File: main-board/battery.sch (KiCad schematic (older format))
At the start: 17 parts, among them Q301 DMG1012T, U301 SX1308, U302 DW06D

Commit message: refactor
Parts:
- added TP301: VBAT, TestPoint:TestPoint_Pad_D1.0mm, symbol Connector:TestPoint
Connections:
- net labels added: BAT_GND
- wire segments 50 -> 51
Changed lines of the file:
@@
 $Descr A4 11693 8268
 encoding utf-8
-Sheet 3 3
+Sheet 3 4
 Title ""
 Date ""
@@
 Text HLabel 6270 2330 2    50   Output ~ 0
 BATTERY_READ
+Text Label 1680 2080 2    50   ~ 0
+BAT_GND
+$Comp
+L Connector:TestPoint TP?
+U 1 1 5DA11FCB
+P 5160 4270
+AR Path="/5DA11FCB" Ref="TP?"  Part="1"
+AR Path="/5DC2722E/5DA11FCB" Ref="TP301"  Part="1"
+F 0 "TP301" V 5230 4440 50  0000 R CNN
+F 1 "VBAT" V 5070 4440 50  0000 R CNN
+F 2 "TestPoint:TestPoint_Pad_D1.0mm" H 5360 4270 50  0001 C CNN
+F 3 "~" H 5360 4270 50  0001 C CNN
+	1    5160 4270
+	0    -1   -1   0
+$EndComp
+Wire Wire Line
+	5160 4270 5360 4270
+Text Label 5190 4270 0    50   ~ 0
+VBAT
 $EndSCHEMATC

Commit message: ALPHA 1
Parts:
- added TP401: +3V3, TestPoint:TestPoint_Pad_D1.0mm, symbol Connector:TestPoint
- renumbered BT301 to BT401, C301 to C401, C303 to C402, C304 to C403, C302 to C404, D301 to D401, L301 to L401, Q301 to Q401, R301 to R401, R302 to R402, R304 to R403, R306 to R404, R307 to R405, R303 to R406, R305 to R407, TP301 to TP402, U301 to U401, U302 to U402
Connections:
- wire segments 51 -> 52
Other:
- moved on the sheet: BT401, C403, C404, Q401, R404, R405, R406, R407, TP402, U402

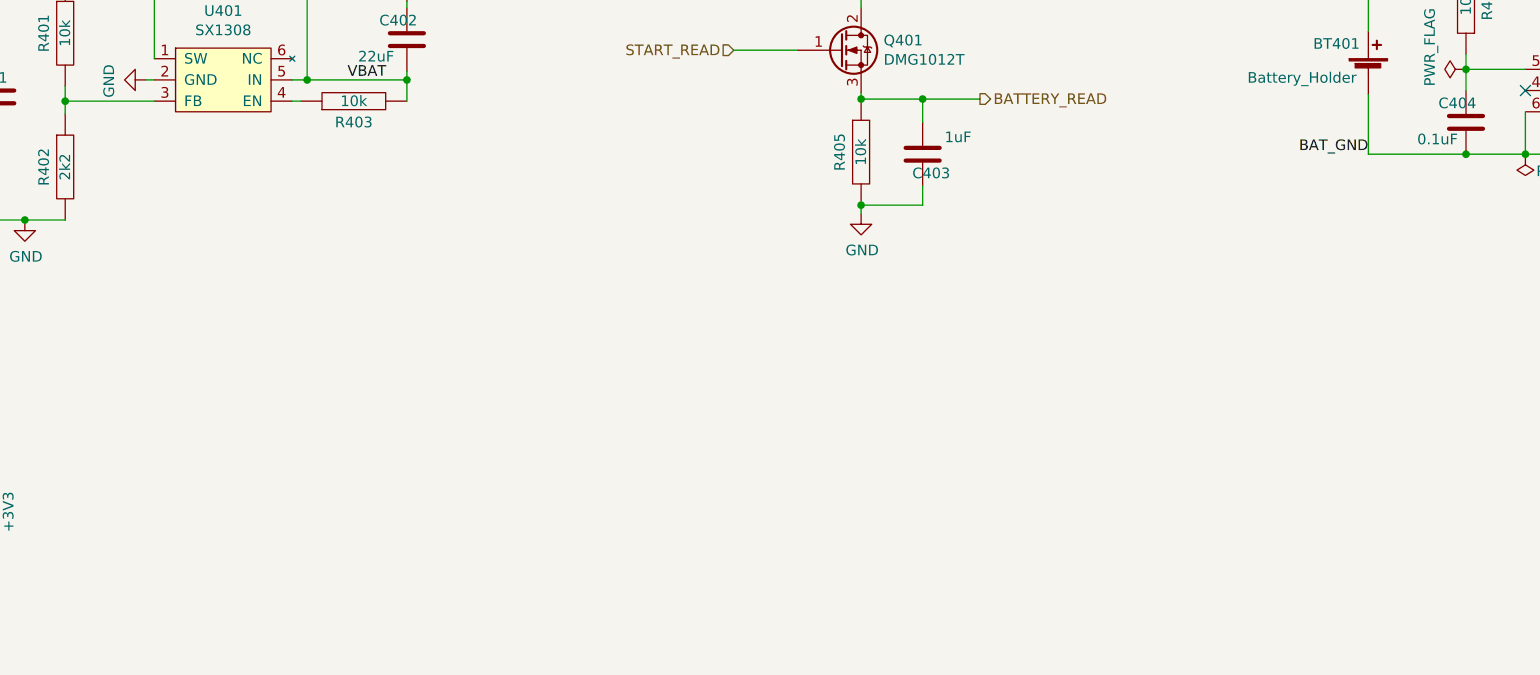
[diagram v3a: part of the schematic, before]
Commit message: added battery charging
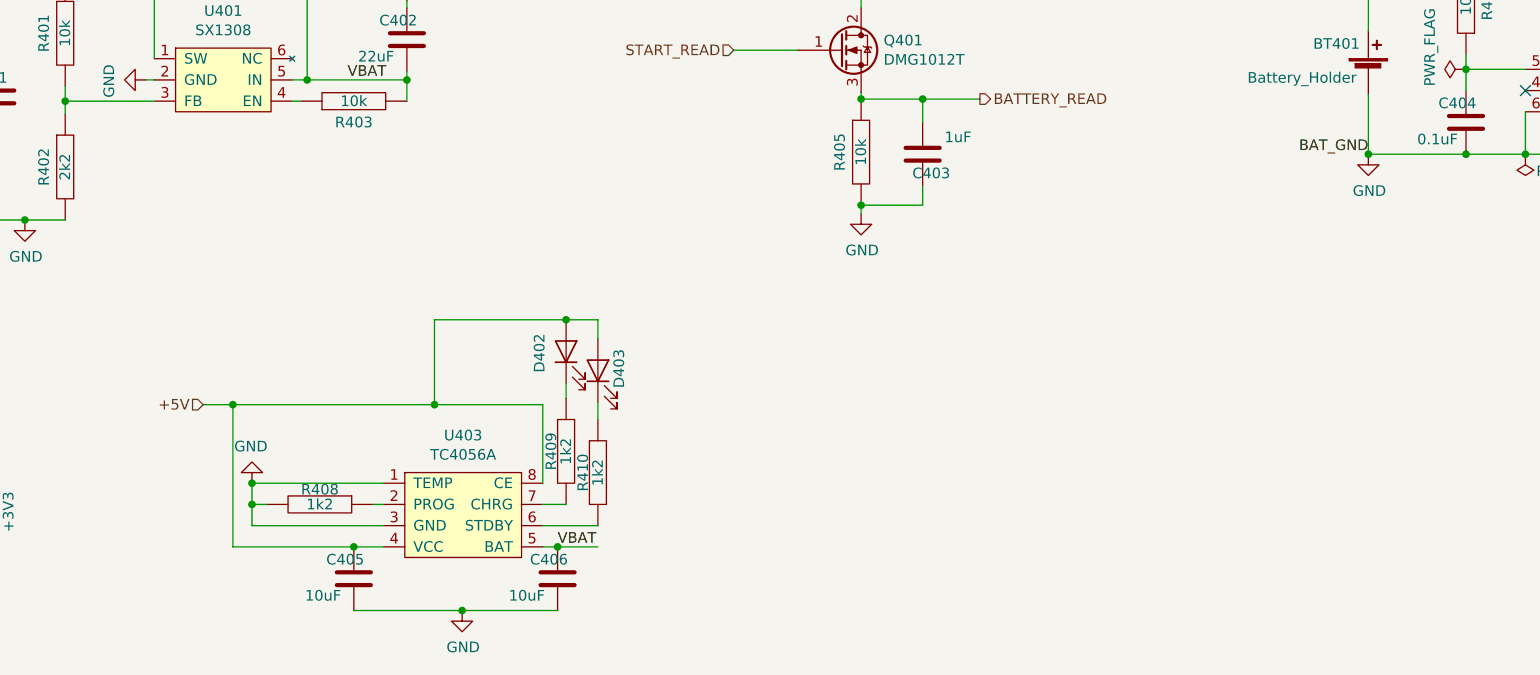
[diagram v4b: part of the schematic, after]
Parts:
- added C405, C406: 10uF, Capacitor_SMD:C_1206_3216Metric_Pad1.42x1.75mm_HandSolder, symbol Device:C
- added D402: RED, LED_SMD:LED_0805_2012Metric_Pad1.15x1.40mm_HandSolder, symbol Device:LED
- added D403: GREEN, LED_SMD:LED_0805_2012Metric_Pad1.15x1.40mm_HandSolder, symbol Device:LED
- added R408, R409, R410: 1k2, Resistor_SMD:R_0805_2012Metric_Pad1.15x1.40mm_HandSolder, symbol pspice:R
- added U403: TC4056A, Package_SO:SOP-8-1EP_4.57x4.57mm_P1.27mm_EP4.57x4.45mm_ThermalVias, symbol water-lib:TC4056A
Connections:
- net BAT_GND is gone; now on net GND: BT401.-, C404.2, U402.3 (S2), U402.6 (VSS)
- net GND: now also C405.2, C406.2, R408.2, U403.1 (TEMP), U403.3 (GND)
- net VBAT: now also C406.1, U403.5 (BAT)
- new net: R408.1, U403.2 (PROG)
- new net: R410.2, U403.6 (STDBY)
- new net: R409.2, U403.7 (CHRG)
- new net: D402.1 (K), R409.1
- new net: D403.1 (K), R410.1
- new net +5V: C405.1, D402.2 (A), D403.2 (A), U403.4 (VCC), U403.8 (CE)
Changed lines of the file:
@@
 Wire Wire Line
 	1440 5820 1520 5820
+Text HLabel 2610 5330 0    50   Input ~ 0
++5V
+$Comp
+L water-lib:TC4056A U403
+U 1 1 5DBA0D54
+P 3810 5800
+F 0 "U403" H 3835 6125 50  0000 C CNN
+F 1 "TC4056A" H 3835 6034 50  0000 C CNN
+F 2 "Package_SO:SOP-8-1EP_4.57x4.57mm_P1.27mm_EP4.57x4.45mm_ThermalVias" H 3910 5250 50  0001 C CNN
+F 3 "https://pdf1.alldatasheet.com/datasheet-pdf/view/1132360/ADMOS/TC4056A.html" H 3960 5350 50  0001 C CNN
+F 4 "C84051" H 3960 6000 50  0001 C CNN "LCSC"
+	1    3810 5800
+	1    0    0    -1
+$EndComp
+Wire Wire Line
+	4210 5700 4210 5330
+Wire Wire Line
+	2750 5330 2610 5330
+Connection ~ 2750 5330
+Wire Wire Line
+	2750 5330 2750 6000
+Wire Wire Line
+	2840 5700 2840 5800
+$Comp
+L pspice:R R?
+U 1 1 5DBBA65B
+P 3160 5800
+AR Path="/5DBBA65B" Ref="R?"  Part="1"
+AR Path="/5DC2722E/5DBBA65B" Ref="R408"  Part="1"
+F 0 "R408" V 3090 5800 50  0000 C CNN
+F 1 "1k2" V 3160 5800 50  0000 C CNN
+F 2 "Resistor_SMD:R_0805_2012Metric_Pad1.15x1.40mm_HandSolder" H 3160 5800 50  0001 C CNN
+F 3 "~" H 3160 5800 50  0001 C CNN
+F 4 "C180849" H 3160 5800 50  0001 C CNN "LCSC"
+	1    3160 5800
+	0    1    1    0
+$EndComp
+Wire Wire Line
+	2840 5900 3460 5900
+Wire Wire Line
+	3460 5800 3410 5800
+Wire Wire Line
+	2910 5800 2840 5800
+Connection ~ 2840 5800
+Wire Wire Line
+	2840 5800 2840 5900
+Wire Wire Line
+	2840 5700 3460 5700
+Wire Wire Line
+	2750 6000 3320 6000
+Wire Wire Line
+	2750 5330 3700 5330
+$Comp
+L Device:LED D?
+U 1 1 5DBCED7D
+P 4320 5080
+AR Path="/5DBCED7D" Ref="D?"  Part="1"
+AR Path="/5DA658CB/5DBCED7D" Ref="D?"  Part="1"
+AR Path="/5DC2722E/5DBCED7D" Ref="D402"  Part="1"
+F 0 "D402" H 4313 5205 50  0000 C CNN
+F 1 "RED" H 4313 5205 50  0001 C CNN
+F 2 "LED_SMD:LED_0805_2012Metric_Pad1.15x1.40mm_HandSolder" H 4320 5080 50  0001 C CNN
+F 3 "~" H 4320 5080 50  0001 C CNN
+F 4 "C94691" H 4320 5080 50  0001 C CNN "LCSC"
+	1    4320 5080
+	0    -1   -1   0
+$EndComp
+$Comp
+L Device:LED D?
+U 1 1 5DBD0159
+P 4470 5170
+AR Path="/5DBD0159" Ref="D?"  Part="1"
+AR Path="/5DA658CB/5DBD0159" Ref="D?"  Part="1"
+AR Path="/5DC2722E/5DBD0159" Ref="D403"  Part="1"
+F 0 "D403" H 4480 5070 50  0000 C CNN
+F 1 "GREEN" H 4463 5295 50  0001 C CNN
+F 2 "LED_SMD:LED_0805_2012Metric_Pad1.15x1.40mm_HandSolder" H 4470 5170 50  0001 C CNN
+F 3 "~" H 4470 5170 50  0001 C CNN
+F 4 "C94691" H 4470 5170 50  0001 C CNN "LCSC"
+	1    4470 5170
+	0    -1   -1   0
+$EndComp
+$Comp
+L pspice:R R?
+U 1 1 5DBD06A0
+P 4320 5550
+AR Path="/5DBD06A0" Ref="R?"  Part="1"
+AR Path="/5DC2722E/5DBD06A0" Ref="R409"  Part="1"
+F 0 "R409" V 4250 5550 50  0000 C CNN
+F 1 "1k2" V 4320 5550 50  0000 C CNN
+F 2 "Resistor_SMD:R_0805_2012Metric_Pad1.15x1.40mm_HandSolder" H 4320 5550 50  0001 C CNN
+F 3 "~" H 4320 5550 50  0001 C CNN
+F 4 "C180849" H 4320 5550 50  0001 C CNN "LCSC"
+	1    4320 5550
+	1    0    0    -1
+$EndComp
+$Comp
+L pspice:R R?
+U 1 1 5DBD1E58
+P 4470 5650
+AR Path="/5DBD1E58" Ref="R?"  Part="1"
+AR Path="/5DC2722E/5DBD1E58" Ref="R410"  Part="1"
+F 0 "R410" V 4400 5650 50  0000 C CNN
+F 1 "1k2" V 4470 5650 50  0000 C CNN
+F 2 "Resistor_SMD:R_0805_2012Metric_Pad1.15x1.40mm_HandSolder" H 4470 5650 50  0001 C CNN
+F 3 "~" H 4470 5650 50  0001 C CNN
+F 4 "C180849" H 4470 5650 50  0001 C CNN "LCSC"
+	1    4470 5650
+	1    0    0    -1
+$EndComp
+Wire Wire Line
+	4210 5800 4320 5800
+Wire Wire Line
+	4210 5900 4470 5900
+Wire Wire Line
+	4320 5300 4320 5230
+Wire Wire Line
+	4470 5400 4470 5320
+Wire Wire Line
+	4470 5020 4470 4930
+Wire Wire Line
+	4470 4930 4320 4930
+Wire Wire Line
+	3700 4930 3700 5330
+Connection ~ 4320 4930
+Wire Wire Line
+	4320 4930 3700 4930
+Connection ~ 3700 5330
+Wire Wire Line
+	3700 5330 4210 5330
+Wire Wire Line
+	4210 6000 4280 6000
+Text Label 4280 6000 0    50   ~ 0
+VBAT
+$Comp
+L power:GND #PWR?
+U 1 1 5DBE55E4
+P 2840 5700
+AR Path="/5DBE55E4" Ref="#PWR?"  Part="1"
+AR Path="/5DC2722E/5DBE55E4" Ref="#PWR0408"  Part="1"
+F 0 "#PWR0408" H 2840 5450 50  0001 C CNN
+F 1 "GND" H 2845 5527 50  0000 C CNN
+F 2 "" H 2840 5700 50  0001 C CNN
+F 3 "" H 2840 5700 50  0001 C CNN
+	1    2840 5700
+	-1   0    0    1
+$EndComp
+Connection ~ 2840 5700
+$Comp
+L power:GND #PWR?
+U 1 1 5DBE6B02
+P 8100 4150
+AR Path="/5DBE6B02" Ref="#PWR?"  Part="1"
+AR Path="/5DC2722E/5DBE6B02" Ref="#PWR0409"  Part="1"
+F 0 "#PWR0409" H 8100 3900 50  0001 C CNN
+F 1 "GND" H 8105 3977 50  0000 C CNN
+F 2 "" H 8100 4150 50  0001 C CNN
+F 3 "" H 8100 4150 50  0001 C CNN
+	1    8100 4150
+	1    0    0    -1
+$EndComp
+Connection ~ 8100 4150
+$Comp
+L Device:C C?
+U 1 1 5DBE9A28
+P 3320 6150
+AR Path="/5DBE9A28" Ref="C?"  Part="1"
+AR Path="/5DC2722E/5DBE9A28" Ref="C405"  Part="1"
+F 0 "C405" H 3190 6240 50  0000 L CNN
+F 1 "10uF" H 3090 6070 50  0000 L CNN
+F 2 "Capacitor_SMD:C_1206_3216Metric_Pad1.42x1.75mm_HandSolder" H 3358 6000 50  0001 C CNN
+F 3 "https://datasheet.lcsc.com/szlcsc/Samsung-Electro-Mechanics-CL31B226KPHNNNE_C87996.pdf" H 3320 6150 50  0001 C CNN
+F 4 "C87996" H 3320 6150 50  0001 C CNN "LCSC"
+	1    3320 6150
+	1    0    0    -1
+$EndComp
+Connection ~ 3320 6000
+Wire Wire Line
+	3320 6000 3460 6000
+$Comp
+L Device:C C?
+U 1 1 5DBEC357
+P 4280 6150
+AR Path="/5DBEC357" Ref="C?"  Part="1"
+AR Path="/5DC2722E/5DBEC357" Ref="C406"  Part="1"
+F 0 "C406" H 4150 6240 50  0000 L CNN
+F 1 "10uF" H 4050 6070 50  0000 L CNN
+F 2 "Capacitor_SMD:C_1206_3216Metric_Pad1.42x1.75mm_HandSolder" H 4318 6000 50  0001 C CNN
+F 3 "https://datasheet.lcsc.com/szlcsc/Samsung-Electro-Mechanics-CL31B226KPHNNNE_C87996.pdf" H 4280 6150 50  0001 C CNN
+F 4 "C87996" H 4280 6150 50  0001 C CNN "LCSC"
+	1    4280 6150
+	1    0    0    -1
+$EndComp
+Connection ~ 4280 6000
+Wire Wire Line
+	4280 6000 4470 6000
+Wire Wire Line
+	3320 6300 3830 6300
+$Comp
+L power:GND #PWR?
+U 1 1 5DBEEA94
+P 3830 6300
+AR Path="/5DBEEA94" Ref="#PWR?"  Part="1"
+AR Path="/5DC2722E/5DBEEA94" Ref="#PWR0410"  Part="1"
+F 0 "#PWR0410" H 3830 6050 50  0001 C CNN
+F 1 "GND" H 3835 6127 50  0000 C CNN
+F 2 "" H 3830 6300 50  0001 C CNN
+F 3 "" H 3830 6300 50  0001 C CNN
+	1    3830 6300
+	1    0    0    -1
+$EndComp
+Connection ~ 3830 6300
+Wire Wire Line
+	3830 6300 4280 6300
 $EndSCHEMATC
